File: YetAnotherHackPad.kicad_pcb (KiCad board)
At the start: 2 copper layers, 71.4 x 73.8 mm, 11 parts, among them SW1 SW_Push, SW2 SW_Push, SW3 SW_Push, SW4 SW_Push, SW5 SW_Push, SW6 SW_Push, SW7 SW_Push, SW8 SW_Push, SW9 SW_Push, U1 XIAO-RP2040-DIP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

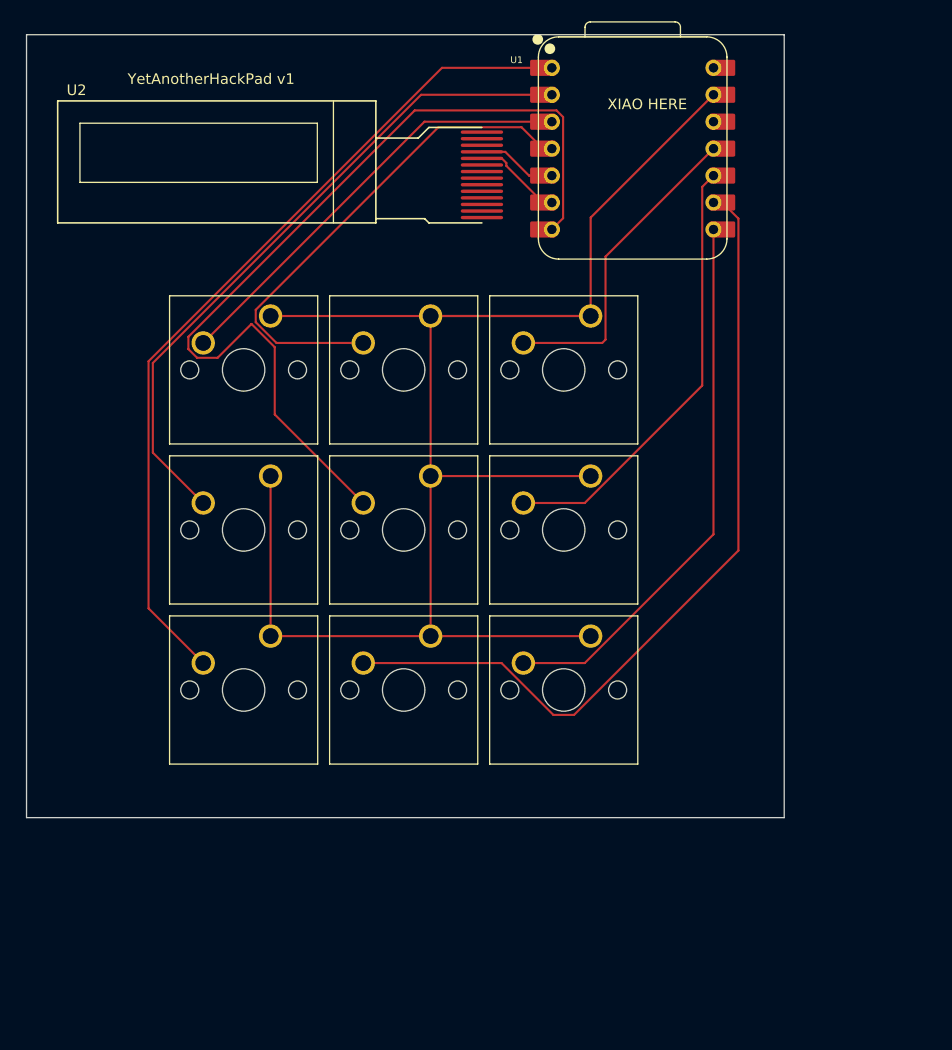
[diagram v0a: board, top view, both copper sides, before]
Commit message: remove unneccesary diodes
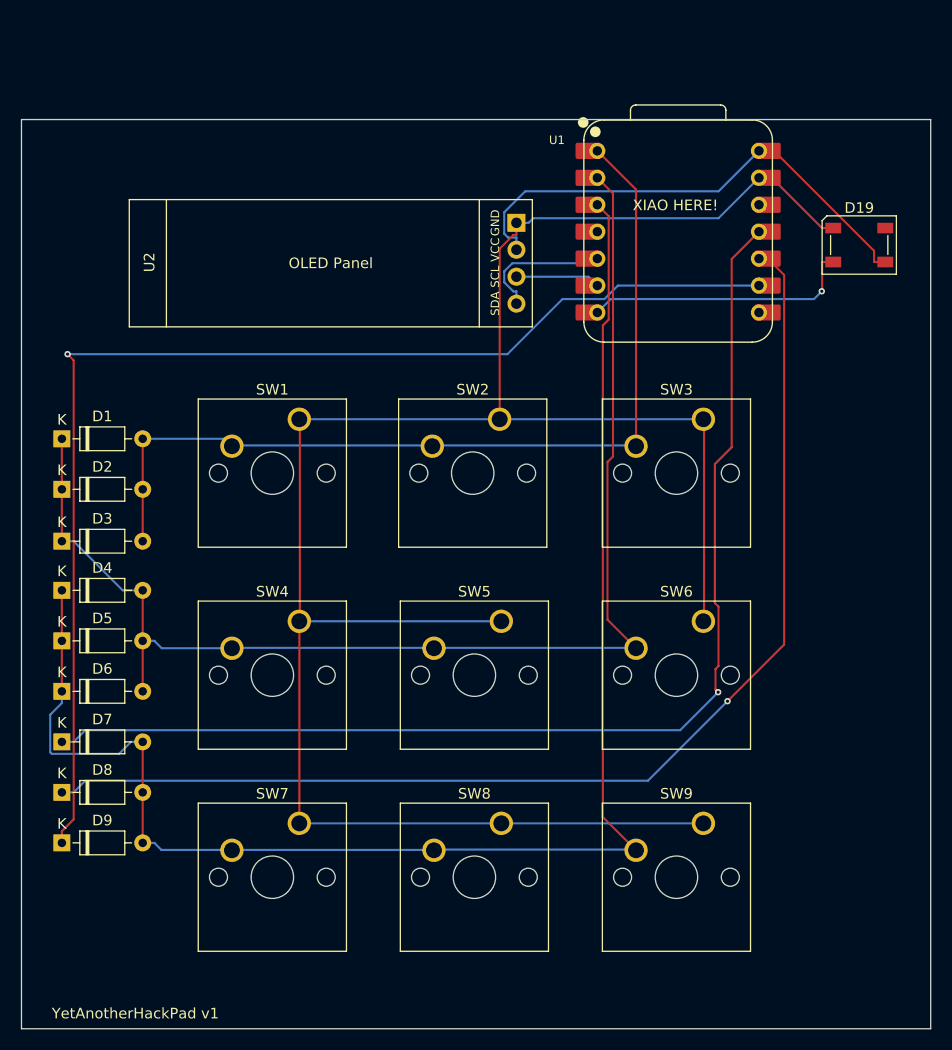
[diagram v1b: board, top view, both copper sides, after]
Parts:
- added D1: D, Diode_THT:D_DO-35_SOD27_P7.62mm_Horizontal, F.Cu at (105.7, 90.5)
- added D19: SK6812, LED_SMD:LED_SK6812_PLCC4_5.0x5.0mm_P3.2mm, F.Cu at (180.9, 72.2)
- added D2: D, Diode_THT:D_DO-35_SOD27_P7.62mm_Horizontal, F.Cu at (105.7, 95.2)
- added D3: D, Diode_THT:D_DO-35_SOD27_P7.62mm_Horizontal, F.Cu at (105.7, 100.1)
- added D4: D, Diode_THT:D_DO-35_SOD27_P7.62mm_Horizontal, F.Cu at (105.7, 104.8)
- added D5: D, Diode_THT:D_DO-35_SOD27_P7.62mm_Horizontal, F.Cu at (105.7, 109.5)
- added D6: D, Diode_THT:D_DO-35_SOD27_P7.62mm_Horizontal, F.Cu at (105.7, 114.3)
- added D7: D, Diode_THT:D_DO-35_SOD27_P7.62mm_Horizontal, F.Cu at (105.7, 119.1)
- added D8: D, Diode_THT:D_DO-35_SOD27_P7.62mm_Horizontal, F.Cu at (105.7, 123.8)
- added D9: D, Diode_THT:D_DO-35_SOD27_P7.62mm_Horizontal, F.Cu at (105.7, 128.6)
- U2: footprint SSD1306_OLED-0.91-128x32:SSD1306_OLED-0.91-128x32 -> KiCad-SSD1306-0.91-OLED-4pin-128x32:SSD1306-0.91-OLED-4pin-128x32
- moved SW7 55.2 mm to (128.1, 126.7)
- moved SW3 45.6 mm to (166.2, 88.6)
- moved SW8 33.8 mm to (147.2, 126.7)
- moved SW4 31.3 mm to (128.1, 107.7)
- moved SW6 25.8 mm to (166.2, 107.7)
- moved SW2 22.3 mm to (147.0, 88.6)
- moved SW9 20.6 mm to (166.2, 126.7)
- moved SW5 15.2 mm to (147.2, 107.7)
- moved U2 11.5 mm to (112.1, 67.9)
- moved SW1 10.1 mm to (128.1, 88.6)
- moved U1 8.93 mm to (163.8, 71.0)
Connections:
- SW1 pad 2: Net-(U1-GPIO28/ADC2/A2) -> Net-(D1-A)
- SW2 pad 2: Net-(U1-GPIO27/ADC1/A1) -> Net-(D1-A)
- SW3 pad 2: Net-(U1-GPIO26/ADC0/A0) -> Net-(D1-A)
- SW4 pad 2: Net-(U1-GPIO29/ADC3/A3) -> Net-(D1-K)
- SW5 pad 2: Net-(U1-GPIO0/TX) -> Net-(D1-K)
- SW6 pad 2: Net-(U1-GPIO2/SCK) -> Net-(D1-K)
- SW7 pad 2: Net-(U1-GPIO3/MOSI) -> Net-(D4-K)
- SW8 pad 2: Net-(U1-GPIO4/MISO) -> Net-(D4-K)
- SW9 pad 2: Net-(U1-GPIO1/RX) -> Net-(D4-K)
- U1 pad 1: Net-(U1-GPIO26/ADC0/A0) -> Net-(D1-A)
- U1 pad 10: Net-(U1-GPIO4/MISO) -> Net-(D8-K)
- U1 pad 11: Net-(U1-GPIO3/MOSI) -> Net-(D7-K)
- U1 pad 2: Net-(U1-GPIO27/ADC1/A1) -> Net-(D1-K)
- U1 pad 3: Net-(U1-GPIO28/ADC2/A2) -> Net-(D4-K)
- U1 pad 4: Net-(U1-GPIO29/ADC3/A3) -> unconnected-(U1-GPIO29/ADC3/A3-Pad4)
- U1 pad 7: Net-(U1-GPIO0/TX) -> Net-(D19-DIN)
- U1 pad 8: Net-(U1-GPIO1/RX) -> unconnected-(U1-GPIO1/RX-Pad8)
- U1 pad 9: Net-(U1-GPIO2/SCK) -> Net-(D9-K)
- U2 pad 1: unconnected-(U2-C2P-Pad1) -> GND
- U2 pad 2: unconnected-(U2-C2N-Pad2) -> +5V
- U2 pad 3: unconnected-(U2-C1P-Pad3) -> Net-(U1-GPIO7/SCL)
- U2 pad 4: unconnected-(U2-C1N-Pad4) -> Net-(U1-GPIO6/SDA)
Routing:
- net Net-(D4-K): track 0.00 -> 145.1 mm
- net Net-(D1-K): track 0.00 -> 122.7 mm
- net Net-(D9-K): track 0.00 -> 115.5 mm, vias 0 -> 1
- net Net-(D8-K): track 0.00 -> 111.7 mm, vias 0 -> 1
- net Net-(D7-K): track 0.00 -> 110.2 mm, vias 0 -> 1
- net Net-(D1-A): track 0.00 -> 86.8 mm
- net Net-(U1-GPIO0/TX): track 85.5 -> 0.00 mm
- net Net-(U1-GPIO26/ADC0/A0): track 80.1 -> 0.00 mm
- net Net-(U1-GPIO2/SCK): track 79.2 -> 0.00 mm
- net Net-(U1-GPIO27/ADC1/A1): track 63.3 -> 0.00 mm
- net Net-(U1-GPIO1/RX): track 51.7 -> 0.00 mm
- net Net-(U1-GPIO29/ADC3/A3): track 48.0 -> 0.00 mm
- net +5V: track 0.00 -> 47.8 mm
- net GND: track 161.5 -> 205.4 mm
- net Net-(U1-GPIO4/MISO): track 41.7 -> 0.00 mm
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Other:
- board size 71.4 x 73.8 mm -> 85.7 x 85.7 mm
- board text added: "XIAO HERE!"
- board text removed: "XIAO HERE"
